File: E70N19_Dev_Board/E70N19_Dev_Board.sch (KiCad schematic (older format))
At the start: 0 parts

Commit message: Begun power connections on ATSAME70N19
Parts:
- added C?: 10pF, symbol C
- added C? (x14): 100nF, symbol C_Small
- added C?: 4.7uF, symbol C_Small
- added C?: 1uF, symbol C_Small
- added L? (x2): 470R @ 100MHz, symbol Ferrite_Bead_Small
- added R?: 5K62, symbol R
- added U?: ATSAME70N19, symbol ATSAME70N19
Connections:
- new net: C?.1, C?.1, C?.1, C?.1, C?.1, C?.1, L?.2, L?.2, U?.18 (VDDCORE), U?.22 (VDDCORE), U?.39 (VDDCORE), U?.4 (VDDOUT), U?.76 (VDDCORE)
- new net: C?.1, L?.1, U?.86 (VDDPLL)
- new net: C?.1, L?.1, U?.96 (VDDUTMIC)
- new net: C?.1, R?.1, U?.97 (VBG)
- new net +3V3: C?.1, C?.1, C?.1, C?.1, C?.1, C?.1, C?.1, C?.1, U?.19 (VDDIO), U?.28 (VDDIO), U?.5 (VDDIN), U?.68 (VDDIO), U?.81 (VDDIO), U?.90 (VDDPLLUSB), U?.93 (VDDUTMII)
- new net GND: C?.2, C?.2, C?.2, C?.2, C?.2, C?.2, C?.2, C?.2, C?.2, C?.2, C?.2, C?.2, C?.2, C?.2, C?.2, C?.2, C?.2, R?.2, U?.10 (GND), U?.29 (GND), U?.3 (GND), U?.67 (GND), U?.7 (GND), U?.8 (GND)

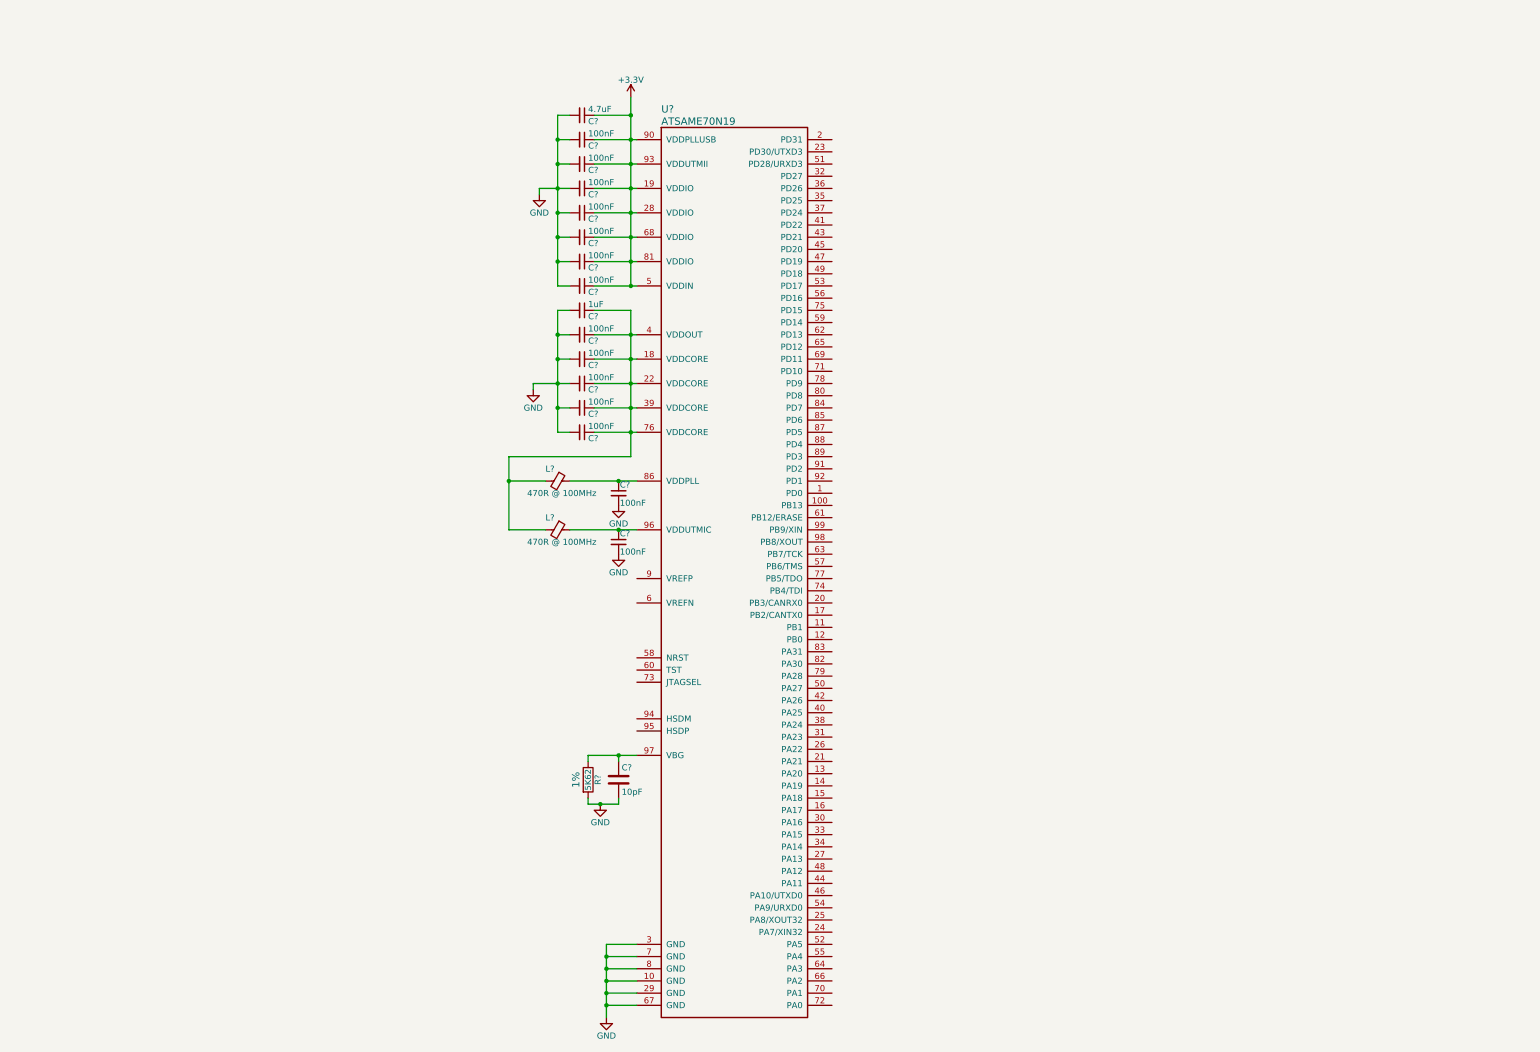
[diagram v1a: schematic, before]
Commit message: Implements power schematic
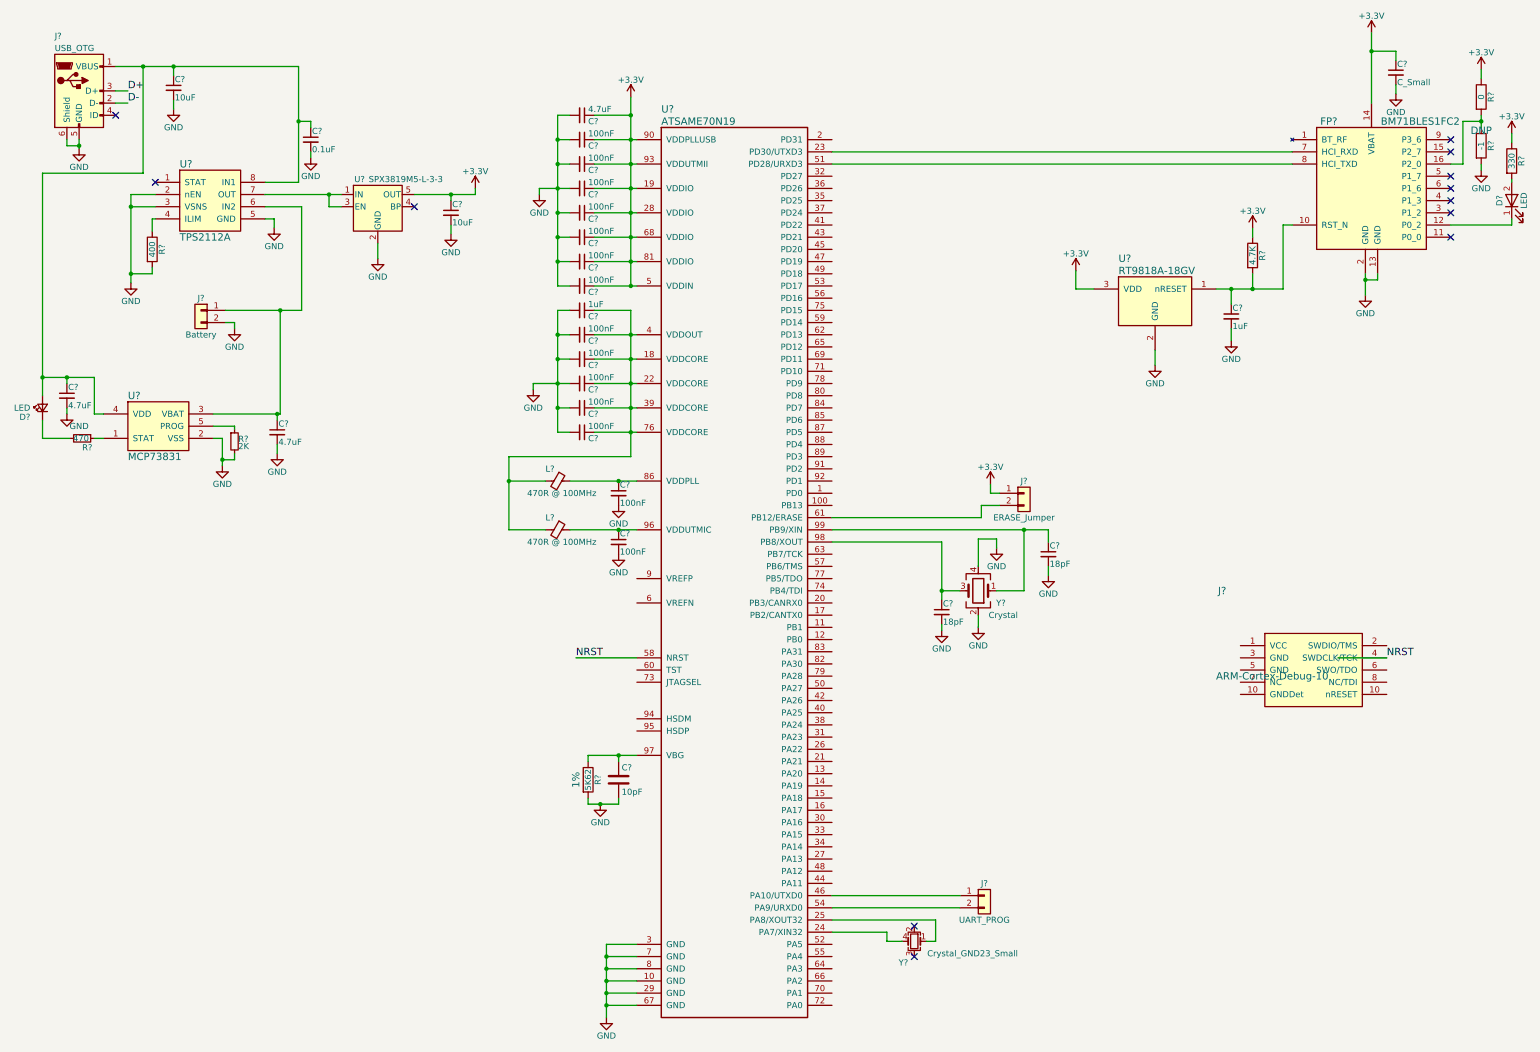
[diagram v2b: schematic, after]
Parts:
- added C?: 1uF, symbol C_Small
- added C?: C_Small, symbol C_Small
- added C? (x2): 10uF, symbol C_Small
- added C?: 0.1uF, symbol C_Small
- added C? (x2): 4.7uF, symbol C_Small
- added C? (x2): 18pF, symbol C_Small
- added D?: LED, symbol LED
- added D?: LED, symbol LED_Small
- added FP?: BM71BLES1FC2, symbol BM71BLES1FC2
- added J?: ARM-Cortex-Debug-10, symbol ARM-Cortex-Debug-10
- added J?: USB_OTG, symbol USB_OTG
- added J?: Battery, Connectors_JST:JST_PH_S2B-PH-SM4-TB_02x2.00mm_Angled, symbol Conn_01x02
- added J?: ERASE_Jumper, symbol Conn_01x02
- added J?: UART_PROG, symbol Conn_01x02
- added R?: 4.7K, symbol R
- added R?: 330, symbol R
- added R?: 0, symbol R
- added R?: -1, symbol R
- added R?: 400, symbol R
- added R?: 2K, symbol R_Small
- added R?: 470, symbol R_Small
- added U?: RT9818A-18GV, symbol RT9818A-18GV
- added U?: TPS2112A, symbol TPS2112A
- added U?: SPX3819M5-L-3-3, TO_SOT_Packages_SMD:SOT-23-5, symbol SPX3819M5-L-3-3
- added U?: MCP73831, symbol MCP73831
- added Y?: Crystal_GND23_Small, symbol Crystal_GND23_Small
- added Y?: Crystal, symbol Crystal_GND24
- L? (x2): Digikey (none) -> 445-5218-1-ND; Fieldname (none) -> Value
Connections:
- net +3V3: now also C?.1, C?.1, FP?.14 (VBAT), J?.1 (Pin_1), R?.1, R?.1, R?.1, U?.3 (VDD), U?.5 (OUT)
- net GND: now also C?.2, C?.2, C?.2, C?.2, C?.2, C?.2, C?.2, C?.2, C?.2, FP?.13 (GND), FP?.2 (GND), J?.2 (Pin_2), J?.5 (GND), J?.6 (Shield), R?.2, R?.2, R?.2, U?.2 (GND), U?.2 (GND), U?.2 (VSS), U?.2 (nEN), U?.3 (VSNS), U?.5 (GND), Y?.2, Y?.4
- net at U?.23 (PD30/UTXD3): now also FP?.7 (HCI_RXD)
- net at U?.24 (PA7/XIN32): now also Y?.4
- net at U?.25 (PA8/XOUT32): now also Y?.1
- net at U?.46 (PA10/UTXD0): now also J?.1 (Pin_1)
- net at U?.51 (PD28/URXD3): now also FP?.8 (HCI_TXD)
- net at U?.54 (PA9/URXD0): now also J?.2 (Pin_2)
- net NRST: now reaches U?.58 (NRST)
- net NRST: now also J?.4 (SWDCLK/TCK)
- net at U?.61 (PB12/ERASE): now also J?.2 (Pin_2)
- net at U?.98 (PB8/XOUT): now also C?.1, Y?.3
- net at U?.99 (PB9/XIN): now also C?.1, Y?.1
- new net: C?.1, FP?.10 (RST_N), R?.2, U?.1 (nRESET)
- new net: D?.1 (K), FP?.12 (P0_2)
- new net: FP?.16 (P2_0), R?.1, R?.2
- new net: D?.2 (A), R?.2
- new net: C?.1, C?.1, C?.1, D?.2 (A), J?.1 (VBUS), U?.4 (VDD), U?.8 (IN1)
- new net: R?.1, U?.4 (ILIM)
- new net: C?.1, J?.1 (Pin_1), U?.3 (VBAT), U?.6 (IN2)
- new net: U?.1 (IN), U?.3 (EN), U?.7 (OUT)
- new net: R?.1, U?.1 (STAT)
- new net: R?.1, U?.5 (PROG)
- new net: D?.1 (K), R?.2
- new net D+: J?.3 (D+)
- new net D-: J?.2 (D-)
- no-connect marks 0 -> 12

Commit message: Finished Schematic
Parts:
- removed J?: ARM-Cortex-Debug-10, symbol ARM-Cortex-Debug-10
- removed J?: ERASE_Jumper, symbol Conn_01x02
- added C26, C28: 100nF, symbol C_Small
- added J3: JTAGSEL_JUMPER, symbol Conn_01x03
- added J5: ERASE_JUMPER, symbol Conn_01x03
- added J6: ARM-Cortex-Debug-10, symbol ARM-Cortex-Debug-10
- added J7: CAN, symbol Conn_01x02
- added J8, J9: Conn_02x15_Counter_Clockwise, symbol Conn_02x15_Counter_Clockwise
- added R10, R11, R9: 100K, symbol R
- added SW1: NRST_BUTTON, symbol SW_Push
- added U6: SN65HVD233-Q1, symbol SN65HVD233-Q1
- gave numbers to parts that had none: 49
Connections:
- net +3V3: now also U4.9 (VREFP), C26.1, C28.1, J3.2 (Pin_2), J5.2 (Pin_2), J6.1 (VCC), R10.1, R11.1, R9.1, SW1.1, U6.3 (VCC)
- net D+: now also U4.95 (HSDP)
- net D-: now also U4.94 (HSDM)
- net GND: now also U4.6 (VREFN), C26.2, C28.2, J6.3 (GND), J6.5 (GND), U6.2 (GND), U6.5 (LBK), U6.8 (RS)
- net NRST: now also J6.10 (nRESET), R11.2, SW1.2
- net PD0: now reaches U4.1 (PD0)
- net PD0: now also J8.1 (Pin_1)
- net PB13: now reaches U4.100 (PB13)
- net PB13: now also J9.29 (Pin_29)
- net PB1: now reaches U4.11 (PB1)
- net PB1: now also J9.28 (Pin_28)
- net PB0: now reaches U4.12 (PB0)
- net PB0: now also J9.27 (Pin_27)
- net PA20: now reaches U4.13 (PA20)
- net PA20: now also J9.16 (Pin_16)
- net PA19: now reaches U4.14 (PA19)
- net PA19: now also J9.15 (Pin_15)
- net PA18: now reaches U4.15 (PA18)
- net PA18: now also J9.14 (Pin_14)
- net PA17: now reaches U4.16 (PA17)
- net PA17: now also J9.13 (Pin_13)
- net CAN_TX: now reaches U4.17 (PB2/CANTX0)
- net CAN_TX: now also U6.1 (TXD)
- net PD31: now reaches U4.2 (PD31)
- net PD31: now also J8.28 (Pin_28)
- net CAN_RX: now reaches U4.20 (PB3/CANRX0)
- net CAN_RX: now also U6.4 (RXD)
- net PA21: now reaches U4.21 (PA21)
- net PA21: now also J9.17 (Pin_17)
- net PA22: now reaches U4.26 (PA22)
- net PA22: now also J9.18 (Pin_18)
- net PA13: now reaches U4.27 (PA13)
- net PA13: now also J9.9 (Pin_9)
- net PA16: now reaches U4.30 (PA16)
- net PA16: now also J9.12 (Pin_12)
- net PA23: now reaches U4.31 (PA23)
- net PA23: now also J9.19 (Pin_19)
- net PD27: now reaches U4.32 (PD27)
- net PD27: now also J8.27 (Pin_27)
- net PA15: now reaches U4.33 (PA15)
- net PA15: now also J9.11 (Pin_11)
- net PA14: now reaches U4.34 (PA14)
- net PA14: now also J9.10 (Pin_10)
- net PD25: now reaches U4.35 (PD25)
- net PD25: now also J8.25 (Pin_25)
- net PD26: now reaches U4.36 (PD26)
- net PD26: now also J8.26 (Pin_26)
- net PD24: now reaches U4.37 (PD24)
- net PD24: now also J8.24 (Pin_24)
- net PA24: now reaches U4.38 (PA24)
- net PA24: now also J9.20 (Pin_20)
- net PA25: now reaches U4.40 (PA25)
- net PA25: now also J9.21 (Pin_21)
- net PD22: now reaches U4.41 (PD22)
- net PD22: now also J8.23 (Pin_23)
- net PA26: now reaches U4.42 (PA26)
- net PA26: now also J9.22 (Pin_22)
- net PD21: now reaches U4.43 (PD21)
- net PD21: now also J8.22 (Pin_22)
- net PA11: now reaches U4.44 (PA11)
- net PA11: now also J9.7 (Pin_7)
- net PD20: now reaches U4.45 (PD20)
- net PD20: now also J8.21 (Pin_21)
- net PD19: now reaches U4.47 (PD19)
- net PD19: now also J8.20 (Pin_20)
- net PA12: now reaches U4.48 (PA12)
- net PA12: now also J9.8 (Pin_8)
- net PD18: now reaches U4.49 (PD18)
- net PD18: now also J8.19 (Pin_19)
- net PA27: now reaches U4.50 (PA27)
- net PA27: now also J9.23 (Pin_23)
- net PA5: now reaches U4.52 (PA5)
- net PA5: now also J9.6 (Pin_6)
- net PD17: now reaches U4.53 (PD17)
- net PD17: now also J8.18 (Pin_18)
- net PA4: now reaches U4.55 (PA4)
- net PA4: now also J9.5 (Pin_5)
- net PD16: now reaches U4.56 (PD16)
- net PD16: now also J8.17 (Pin_17)
- net TMS: now reaches U4.57 (PB6/TMS)
- net TMS: now also J6.2 (SWDIO/TMS), R9.2
- net PD14: now reaches U4.59 (PD14)
- net PD14: now also J8.15 (Pin_15)
- net at U4.61 (PB12/ERASE): now also J5.3 (Pin_3)
- net PD13: now reaches U4.62 (PD13)
- net PD13: now also J8.14 (Pin_14)
- net TCK: now reaches U4.63 (PB7/TCK)
- net TCK: now also J6.4 (SWDCLK/TCK), R10.2
- net PA3: now reaches U4.64 (PA3)
- net PA3: now also J9.4 (Pin_4)
- net PD12: now reaches U4.65 (PD12)
- net PD12: now also J8.13 (Pin_13)
- net PA2: now reaches U4.66 (PA2)
- net PA2: now also J9.3 (Pin_3)
- net PD11: now reaches U4.69 (PD11)
- net PD11: now also J8.12 (Pin_12)
- net PA1: now reaches U4.70 (PA1)
- net PA1: now also J9.2 (Pin_2)
- net PD10: now reaches U4.71 (PD10)
- net PD10: now also J8.11 (Pin_11)
- net PA0: now reaches U4.72 (PA0)
- net PA0: now also J9.1 (Pin_1)
- net at U4.73 (JTAGSEL): now also J3.1 (Pin_1)
- net PD15: now reaches U4.75 (PD15)
- net PD15: now also J8.16 (Pin_16)
- net TDO: now reaches U4.77 (PB5/TDO)
- net TDO: now also J6.6 (SWO/TDO)
- net PD9: now reaches U4.78 (PD9)
- net PD9: now also J8.10 (Pin_10)
- net PA28: now reaches U4.79 (PA28)
- net PA28: now also J9.24 (Pin_24)
- net PD8: now reaches U4.80 (PD8)
- net PD8: now also J8.9 (Pin_9)
- net PA30: now reaches U4.82 (PA30)
- net PA30: now also J9.25 (Pin_25)
- net PA31: now reaches U4.83 (PA31)
- net PA31: now also J9.26 (Pin_26)
- net PD7: now reaches U4.84 (PD7)
- net PD7: now also J8.8 (Pin_8)
- net PD6: now reaches U4.85 (PD6)
- net PD6: now also J8.7 (Pin_7)
- net PD5: now reaches U4.87 (PD5)
- net PD5: now also J8.6 (Pin_6)
- net PD4: now reaches U4.88 (PD4)
- net PD4: now also J8.5 (Pin_5)
- net PD3: now reaches U4.89 (PD3)
- net PD3: now also J8.4 (Pin_4)
- net PD2: now reaches U4.91 (PD2)
- net PD2: now also J8.3 (Pin_3)
- net PD1: now reaches U4.92 (PD1)
- net PD1: now also J8.2 (Pin_2)
- new net: J7.1 (Pin_1), U6.~ (CANH)
- new net: J7.2 (Pin_2), U6.6 (CANL)
- no-connect marks 12 -> 22
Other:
- note added: "Bluetooth Module\n"
- note added: "CAN Transceiver"
- note added: "GPIO Breakout\n"
- note added: "JTAG Interface\n"
- note added: "Power Input and Regulation"

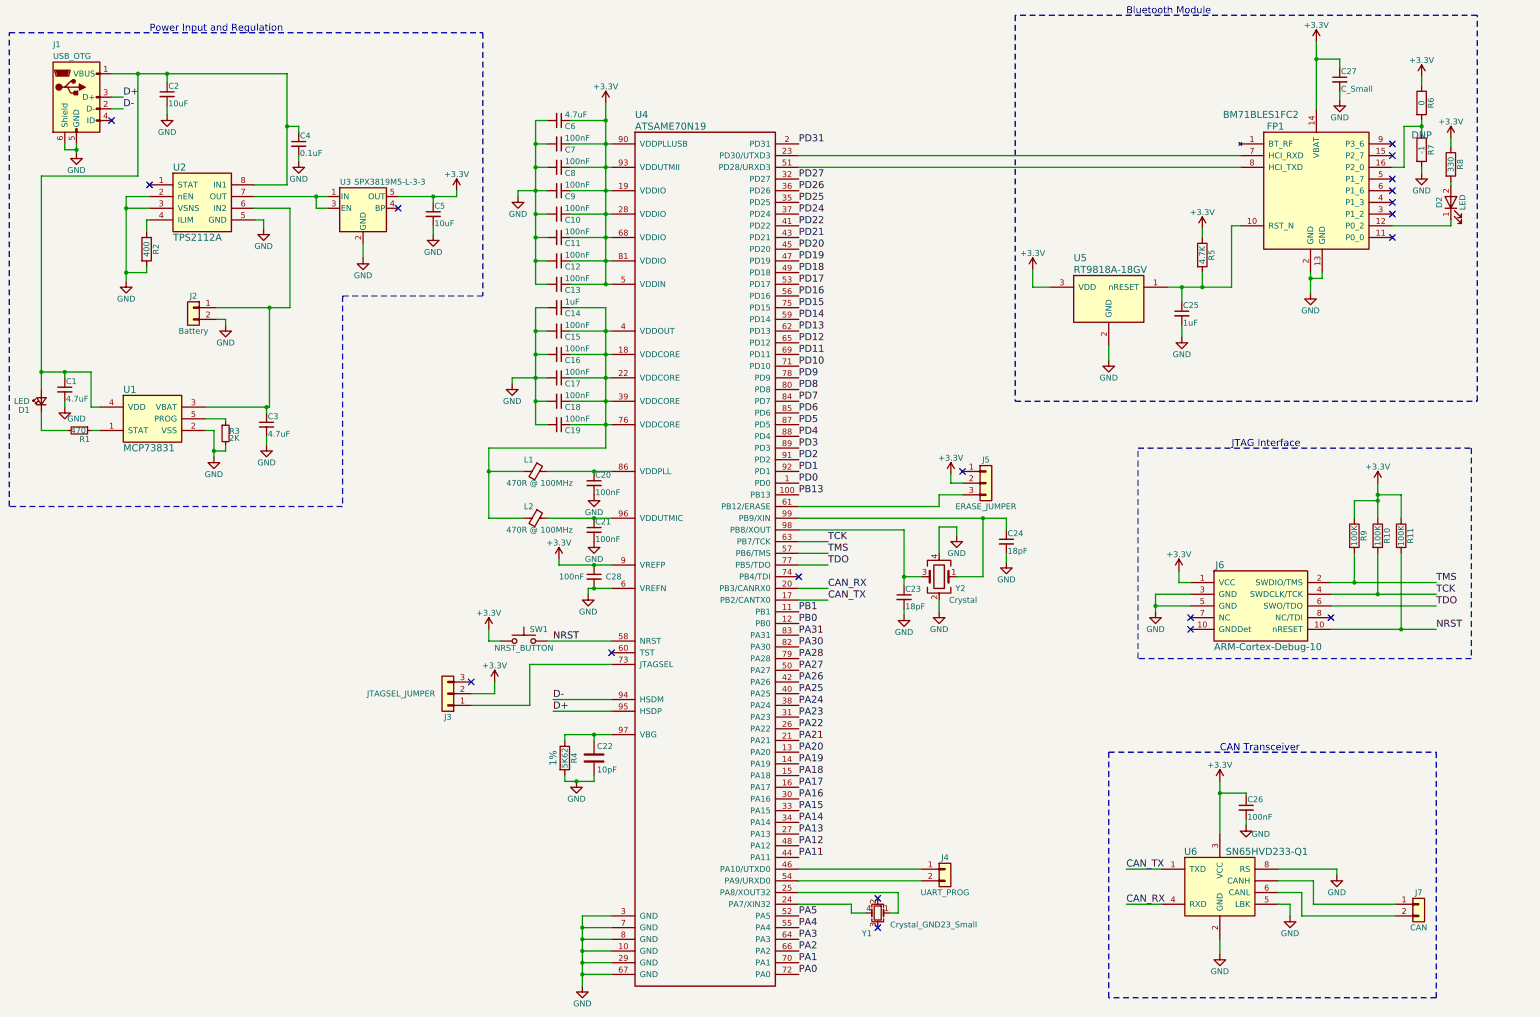
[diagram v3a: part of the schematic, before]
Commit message: Updating schematic with corrected values
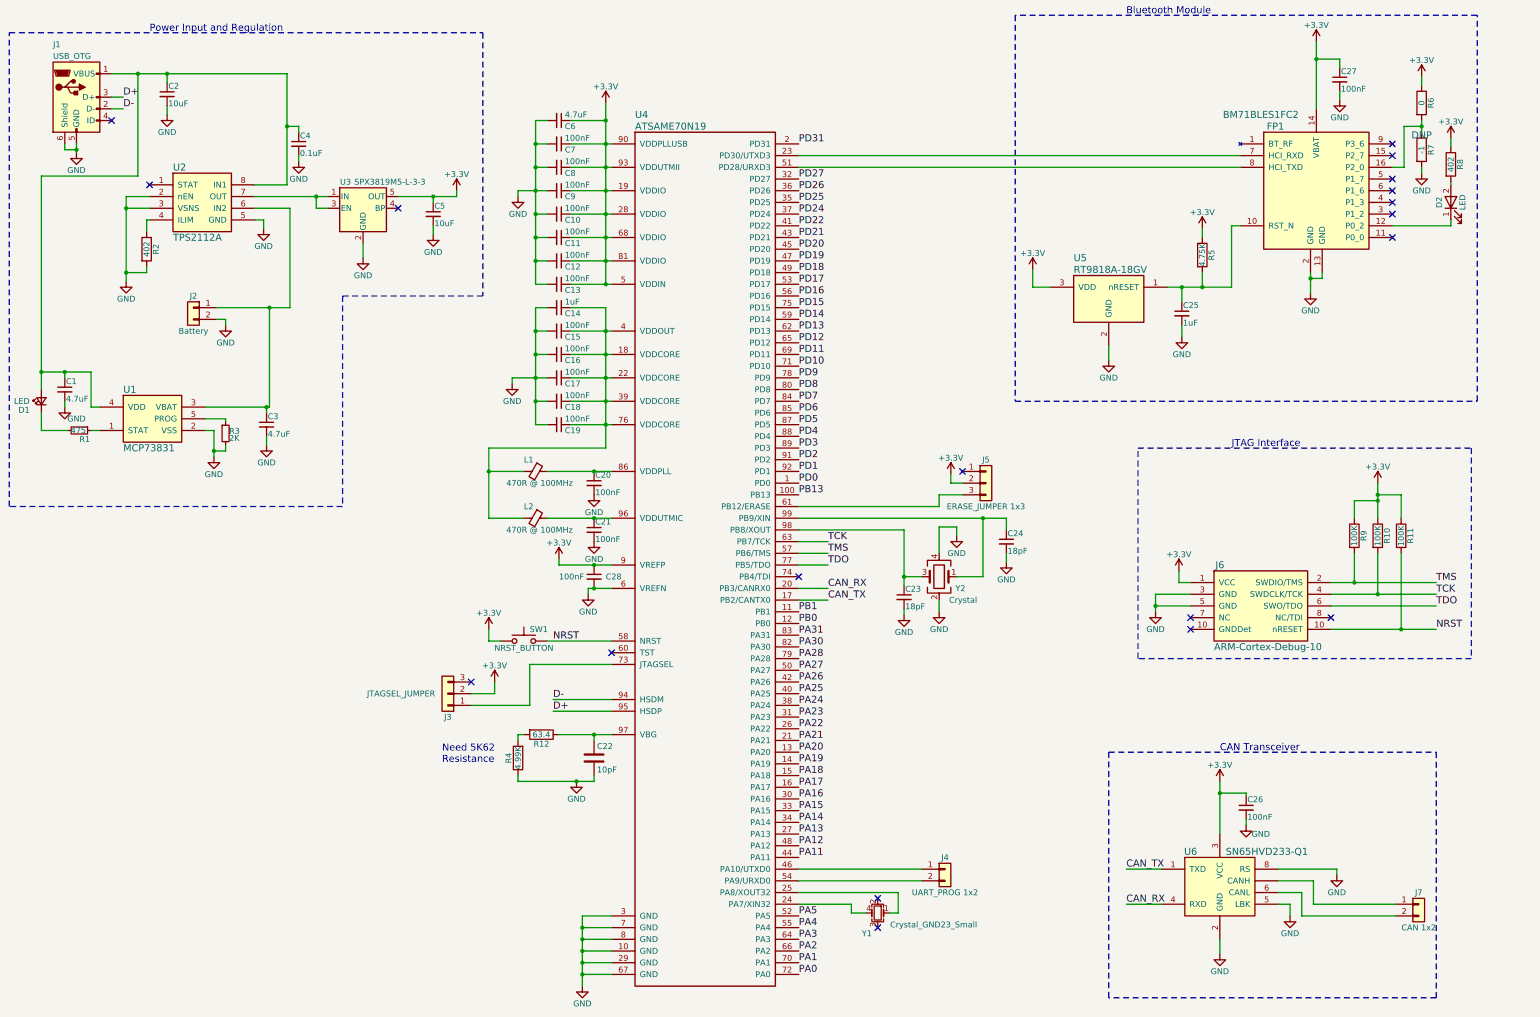
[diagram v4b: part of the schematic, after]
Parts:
- added R12: 63.4, symbol R
- C27: value C_Small -> 100nF; Fieldname (none) -> Value
- J4: value UART_PROG -> UART_PROG 1x2
- J5: value ERASE_JUMPER -> ERASE_JUMPER 1x3; Fieldname (none) -> Value
- J7: value CAN -> CAN 1x2; Fieldname (none) -> Value
- R1: value 470 -> 475
- R2: value 400 -> 402
- R4: value 5K62 -> 4.99K; Fieldname (none) -> Value; Tolerance 1% -> (none)
- R5: value 4.7K -> 4.75K
- R8: value 330 -> 402
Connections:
- net GND: now also R4.1; no longer R4.2
- net at C22.1, U4.97 (VBG): now also R12.1; no longer R4.1
- new net: R12.2, R4.2
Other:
- note added: "Need 5K62\nResistance\n"

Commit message: Finishing BoM and other requirements
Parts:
- J2: value Battery -> Battery 1x2
- J3: value JTAGSEL_JUMPER -> JTAGSEL_JUMPER 1x3
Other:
- moved on the sheet: J1
